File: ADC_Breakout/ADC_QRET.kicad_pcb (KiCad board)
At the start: 2 copper layers, 80.5 x 74 mm, 33 parts, among them J1 Screw_Terminal_01x03, J2 Screw_Terminal_01x04, J3 Screw_Terminal_01x04, J4 Screw_Terminal_01x04, J5 Screw_Terminal_01x04, U1 ESP32-S3-DEVKITC-1-N8R2

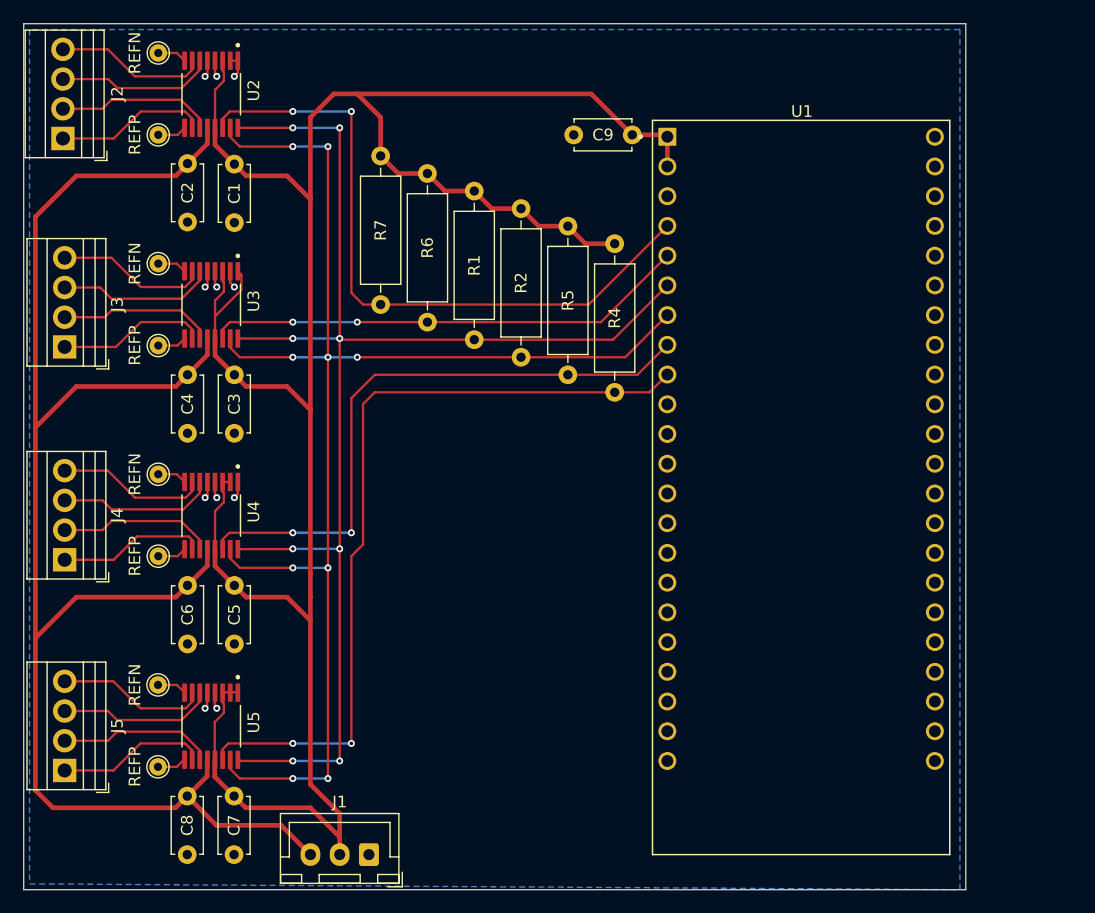
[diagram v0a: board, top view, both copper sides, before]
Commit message: Updated silkscreen
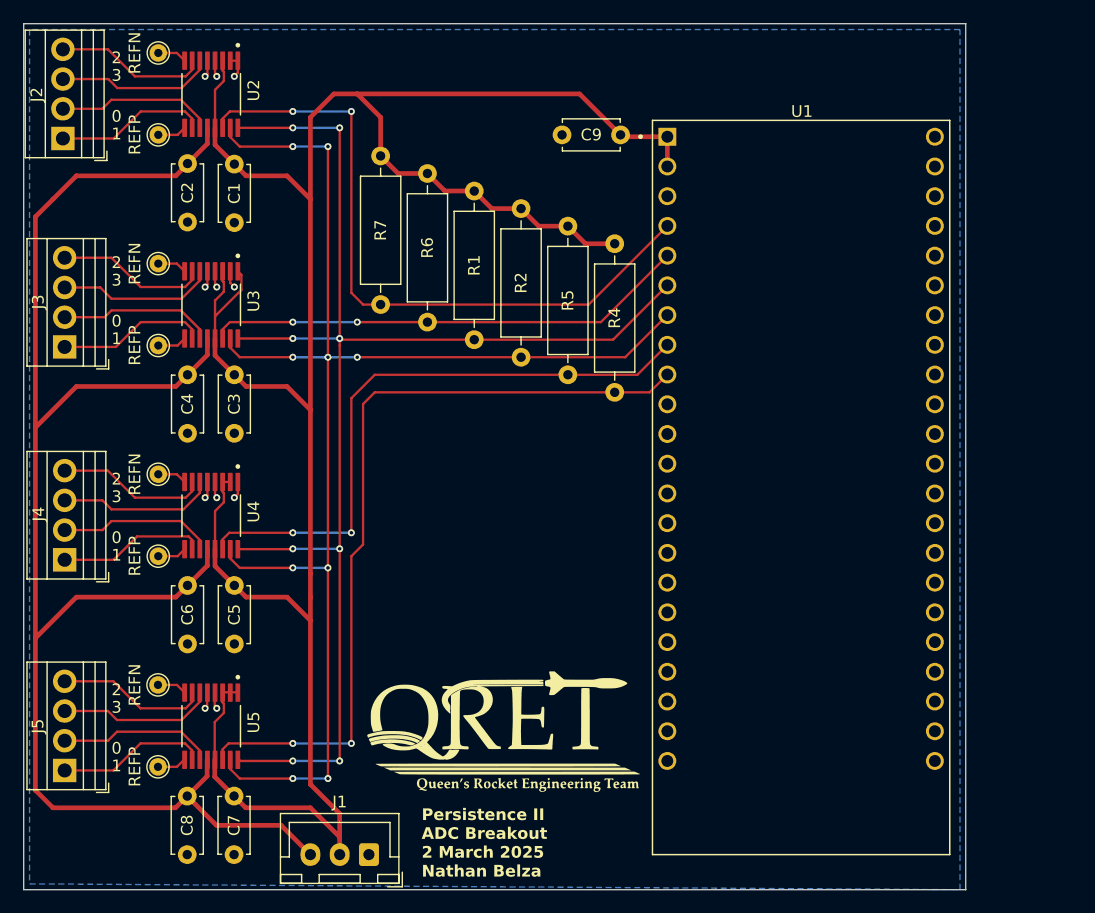
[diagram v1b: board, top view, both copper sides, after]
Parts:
- added G***: LOGO, LOGO, F.Cu at (140.2, 109.1)
- moved C9 1.00 mm to (146.0, 57.5)
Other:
- board text added: "0"
- board text added: "1"
- board text added: "2"
- board text added: "3"
- board text added: "Persistence II ADC Breakout 2 March 2025 Nathan Belza"

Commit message: Added ESP32 IO Terminals
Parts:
- added J6: Screw_Terminal_01x04, TerminalBlock:TerminalBlock_Xinya_XY308-2.54-4P_1x04_P2.54mm_Horizontal, F.Cu at (186.0, 58.1)
- added J7: Screw_Terminal_01x04, TerminalBlock:TerminalBlock_Xinya_XY308-2.54-4P_1x04_P2.54mm_Horizontal, F.Cu at (186.0, 70.0)
- added J8: Screw_Terminal_01x04, TerminalBlock:TerminalBlock_Xinya_XY308-2.54-4P_1x04_P2.54mm_Horizontal, F.Cu at (186.0, 82.0)
- added J9: Screw_Terminal_01x04, TerminalBlock:TerminalBlock_Xinya_XY308-2.54-4P_1x04_P2.54mm_Horizontal, F.Cu at (186.0, 94.1)
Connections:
- U1 pad J3_10: unconnected-(U1-GPIO38-PadJ3_10) -> Net-(J8-Pin_4)
- U1 pad J3_11: unconnected-(U1-GPIO37-PadJ3_11) -> Net-(J8-Pin_3)
- U1 pad J3_12: unconnected-(U1-GPIO36-PadJ3_12) -> Net-(J8-Pin_2)
- U1 pad J3_13: unconnected-(U1-GPIO35-PadJ3_13) -> Net-(J8-Pin_1)
- U1 pad J3_14: unconnected-(U1-GPIO0-PadJ3_14) -> Net-(J9-Pin_1)
- U1 pad J3_15: unconnected-(U1-GPIO45-PadJ3_15) -> Net-(J9-Pin_2)
- U1 pad J3_16: unconnected-(U1-GPIO48-PadJ3_16) -> Net-(J9-Pin_3)
- U1 pad J3_17: unconnected-(U1-GPIO47-PadJ3_17) -> Net-(J9-Pin_4)
- U1 pad J3_2: unconnected-(U1-U0TXD/GPIO43-PadJ3_2) -> Net-(J6-Pin_1)
- U1 pad J3_3: unconnected-(U1-U0RXD/GPIO44-PadJ3_3) -> Net-(J6-Pin_2)
- U1 pad J3_4: unconnected-(U1-GPIO1-PadJ3_4) -> Net-(J6-Pin_3)
- U1 pad J3_5: unconnected-(U1-GPIO2-PadJ3_5) -> Net-(J6-Pin_4)
- U1 pad J3_6: unconnected-(U1-MTMS/GPIO42-PadJ3_6) -> Net-(J7-Pin_4)
- U1 pad J3_7: unconnected-(U1-MTDI/GPIO41-PadJ3_7) -> Net-(J7-Pin_3)
- U1 pad J3_8: unconnected-(U1-MTDO/GPIO40-PadJ3_8) -> Net-(J7-Pin_2)
- U1 pad J3_9: unconnected-(U1-MTCK/GPIO39-PadJ3_9) -> Net-(J7-Pin_1)
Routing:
- net Net-(J9-Pin_4): track 0.00 -> 9.55 mm
- net Net-(J9-Pin_2): track 0.00 -> 9.55 mm
- net Net-(J9-Pin_3): track 0.00 -> 9.55 mm
- net Net-(J9-Pin_1): track 0.00 -> 9.55 mm
- net Net-(J6-Pin_3): track 0.00 -> 9.02 mm
- net Net-(J6-Pin_2): track 0.00 -> 9.02 mm
- net Net-(J6-Pin_1): track 0.00 -> 9.02 mm
- net Net-(J6-Pin_4): track 0.00 -> 9.02 mm
- net Net-(J8-Pin_4): track 0.00 -> 8.77 mm
- net Net-(J8-Pin_2): track 0.00 -> 8.77 mm
- net Net-(J8-Pin_3): track 0.00 -> 8.77 mm
- net Net-(J8-Pin_1): track 0.00 -> 8.77 mm
- net Net-(J7-Pin_4): track 0.00 -> 8.29 mm
- net Net-(J7-Pin_3): track 0.00 -> 8.29 mm
- net Net-(J7-Pin_2): track 0.00 -> 8.29 mm
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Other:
- board size 80.5 x 74 mm -> 89.5 x 74 mm
- board text added: "35"
- board text added: "36"
- board text added: "37"
- board text added: "38"
- board text added: "39"
- board text added: "40"
- board text added: "41"
- board text added: "42"
- board text added: "43"
- board text added: "44"
- board text added: "45"
- board text added: "47"
- board text added: "48"

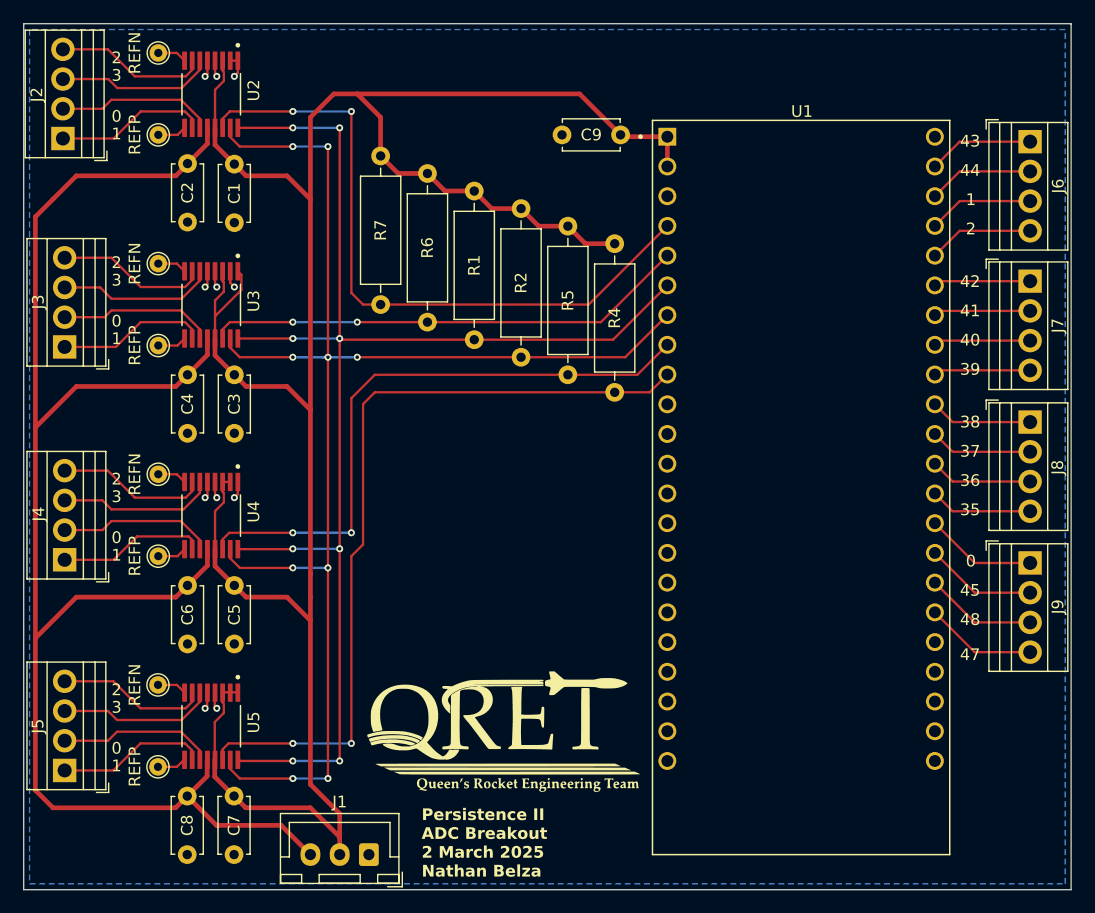
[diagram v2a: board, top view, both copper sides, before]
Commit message: Added standoff holes
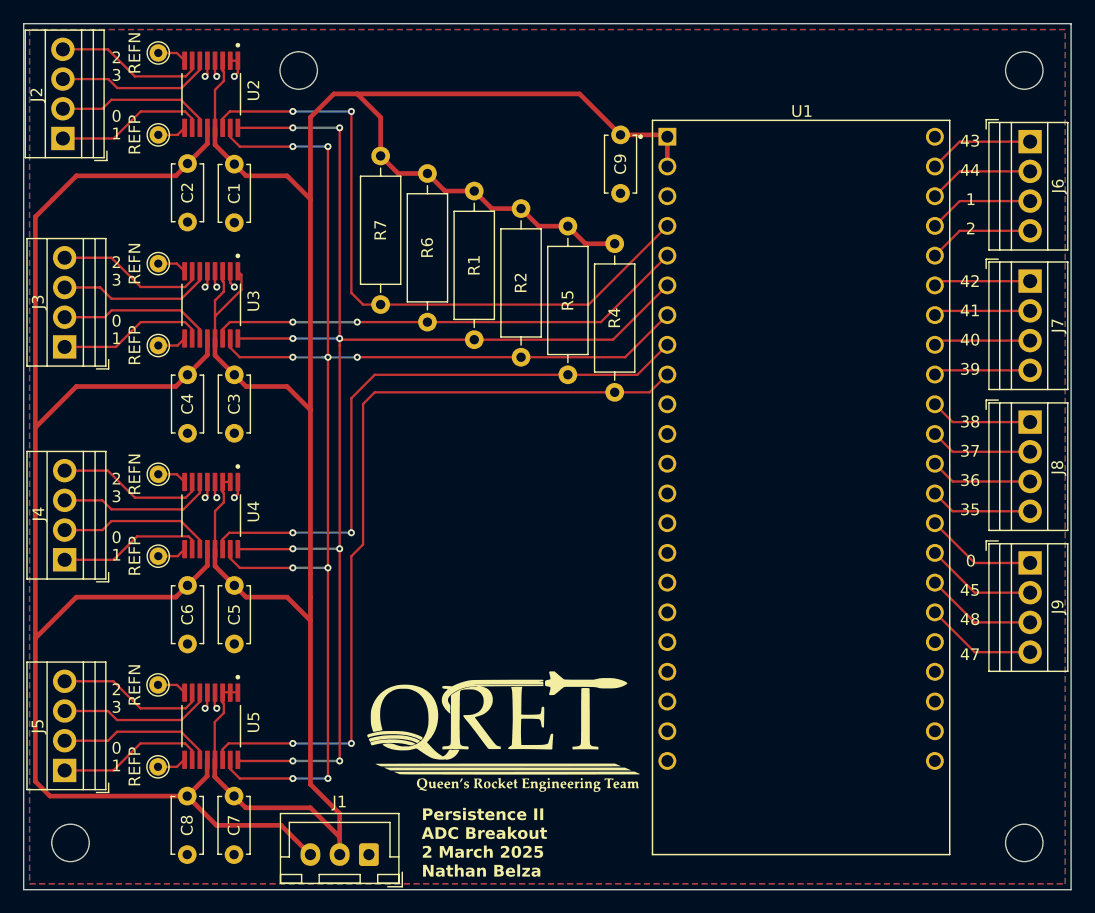
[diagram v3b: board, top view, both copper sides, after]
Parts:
- added H1: MountingHole, MountingHole:MountingHole_3.2mm_M3_DIN965, F.Cu at (185.5, 52.0)
- added H1: MountingHole, MountingHole:MountingHole_3.2mm_M3_DIN965, F.Cu at (123.5, 52.0)
- added H1: MountingHole, MountingHole:MountingHole_3.2mm_M3_DIN965, F.Cu at (104.0, 118.0)
- added H1: MountingHole, MountingHole:MountingHole_3.2mm_M3_DIN965, F.Cu at (185.5, 118.0)
- moved C9 7.07 mm to (151.0, 62.5), turned to 90 degrees
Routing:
- net +5V: track 135.4 -> 134.2 mm
- added copper zone on F.Cu, net GND
